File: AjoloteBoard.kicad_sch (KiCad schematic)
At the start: 4 parts, among them SW1 On

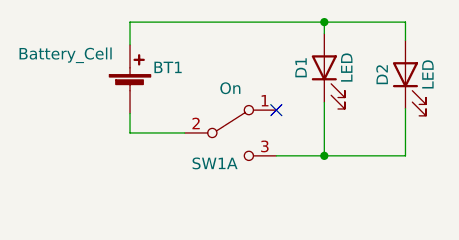
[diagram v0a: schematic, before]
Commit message: Battery holder and switch changed
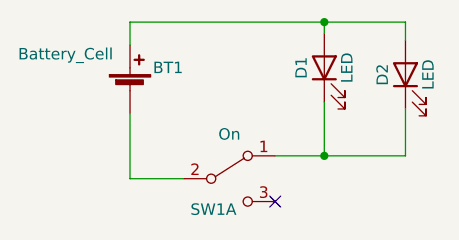
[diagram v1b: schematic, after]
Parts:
- BT1: footprint footprints:79523141 -> Batteries:BAT-HLD-001; manf# (none) -> BAT-HLD-001
- D1, D2: manf# (none) -> Generic LED
- SW1: footprint footprints:Micro_interruptor_SPDT -> footprints:JS102011SAQN; manf# (none) -> JS102011SAQN
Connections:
- net at D1.1 (K), D2.1 (K): now also SW1.1 (A); no longer SW1.3 (C)
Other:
- moved on the sheet: SW1A
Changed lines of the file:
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@@
-(kicad_sch (version 20211123) (generator eeschema)
+(kicad_sch (version 20230121) (generator eeschema)
   (paper "A4")
   (title_block
@@
   (junction (at 120.523 88.265) (diameter 0) (color 0 0 0 0)
   )
-  (no_connect (at 115.189 83.185))
-  (wire (pts (xy 115.189 88.265) (xy 120.523 88.265))
-    (stroke (width 0) (type default) (color 0 0 0 0))
+  (no_connect (at 115.062 93.345))
+  (wire (pts (xy 120.523 88.265) (xy 129.54 88.265))
+    (stroke (width 0) (type default))
   )
-  (wire (pts (xy 120.523 88.265) (xy 129.54 88.265))
-    (stroke (width 0) (type default) (color 0 0 0 0))
+  (wire (pts (xy 115.062 88.265) (xy 120.523 88.265))
+    (stroke (width 0) (type default))
   )
   (wire (pts (xy 129.54 88.265) (xy 129.54 83.058))
-    (stroke (width 0) (type default) (color 0 0 0 0))
+    (stroke (width 0) (type default))
   )
   (wire (pts (xy 120.523 74.676) (xy 120.523 73.406))
-    (stroke (width 0) (type default) (color 0 0 0 0))
+    (stroke (width 0) (type default))
   )
   (wire (pts (xy 120.523 88.265) (xy 120.523 82.296))
-    (stroke (width 0) (type default) (color 0 0 0 0))
+    (stroke (width 0) (type default))
   )
   (wire (pts (xy 129.54 73.406) (xy 129.54 75.438))
-    (stroke (width 0) (type default) (color 0 0 0 0))
+    (stroke (width 0) (type default))
   )
   (wire (pts (xy 98.933 75.946) (xy 98.933 73.406))
-    (stroke (width 0) (type default) (color 0 0 0 0))
+    (stroke (width 0) (type default))
   )
-  (wire (pts (xy 98.933 85.725) (xy 105.029 85.725))
-    (stroke (width 0) (type default) (color 0 0 0 0))
+  (wire (pts (xy 98.933 90.805) (xy 104.902 90.805))
+    (stroke (width 0) (type default))
   )
   (wire (pts (xy 98.933 73.406) (xy 120.523 73.406))
-    (stroke (width 0) (type default) (color 0 0 0 0))
+    (stroke (width 0) (type default))
   )
   (wire (pts (xy 120.523 73.406) (xy 129.54 73.406))
-    (stroke (width 0) (type default) (color 0 0 0 0))
+    (stroke (width 0) (type default))
   )
-  (wire (pts (xy 98.933 83.566) (xy 98.933 85.725))
-    (stroke (width 0) (type default) (color 0 0 0 0))
+  (wire (pts (xy 98.933 83.566) (xy 98.933 90.805))
+    (stroke (width 0) (type default))
   )
   (symbol (lib_id "Device:LED") (at 120.523 78.486 90) (unit 1)
-    (in_bom yes) (on_board yes)
-    (property "Reference" "D1" (id 0) (at 117.983 78.486 0))
-    (property "Value" "LED" (id 1) (at 123.063 78.486 0))
-    (property "Footprint" "LED_THT:LED_D5.0mm_Clear" (id 2) (at 120.523 78.486 0)
+    (in_bom yes) (on_board yes) (dnp no)
+    (property "Reference" "D1" (at 117.983 78.486 0)
+      (effects (font (size 1.27 1.27)))
+    )
+    (property "Value" "LED" (at 123.063 78.486 0)
+      (effects (font (size 1.27 1.27)))
+    )
+    (property "Footprint" "LED_THT:LED_D5.0mm_Clear" (at 120.523 78.486 0)
       (effects (font (size 1.27 1.27)) hide)
     )
-    (property "Datasheet" "" (id 3) (at 120.523 78.486 0))
+    (property "Datasheet" "https://articulo.mercadolibre.com.mx/MLM-849097961-100-led-rgb-camaleon-5mm-parpadeo-rapido-_JM#position=5&search_layout=stack&type=item&tracking_id=6f6aec30-ba55-4563-a3d2-df7b4841300a" (at 120.523 78.486 0)
+      (effects (font (size 1.27 1.27)) hide)
+    )
+    (property "LCSC#" "" (at 120.523 78.486 0)
+      (effects (font (size 1.27 1.27)) hide)
+    )
+    (property "manf#" "Generic LED" (at 120.523 78.486 0)
+      (effects (font (size 1.27 1.27)) hide)
+    )
     (pin "1")
     (pin "2")
+    (instances
+      (project "AjoloteBoard"
+        (path "/7f3eb118-a20c-4239-b800-c9211c66847d"
+          (reference "D1") (unit 1)
+        )
+      )
+    )
   )
   (symbol (lib_id "Device:LED") (at 129.54 79.248 90) (unit 1)
-    (in_bom yes) (on_board yes)
-    (property "Reference" "D2" (id 0) (at 127 79.248 0))
-    (property "Value" "LED" (id 1) (at 132.08 79.248 0))
-    (property "Footprint" "LED_THT:LED_D5.0mm_Clear" (id 2) (at 129.54 79.248 0)
+    (in_bom yes) (on_board yes) (dnp no)
+    (property "Reference" "D2" (at 127 79.248 0)
+      (effects (font (size 1.27 1.27)))
+    )
+    (property "Value" "LED" (at 132.08 79.248 0)
+      (effects (font (size 1.27 1.27)))
+    )
+    (property "Footprint" "LED_THT:LED_D5.0mm_Clear" (at 129.54 79.248 0)
       (effects (font (size 1.27 1.27)) hide)
     )
-    (property "Datasheet" "" (id 3) (at 129.54 79.248 0))
+    (property "Datasheet" "https://articulo.mercadolibre.com.mx/MLM-849097961-100-led-rgb-camaleon-5mm-parpadeo-rapido-_JM#position=5&search_layout=stack&type=item&tracking_id=6f6aec30-ba55-4563-a3d2-df7b4841300a" (at 129.54 79.248 0)
+      (effects (font (size 1.27 1.27)) hide)
+    )
+    (property "LCSC#" "" (at 129.54 79.248 0)
+      (effects (font (size 1.27 1.27)) hide)
+    )
+    (property "manf#" "Generic LED" (at 129.54 79.248 0)
+      (effects (font (size 1.27 1.27)) hide)
+    )
     (pin "1")
     (pin "2")
+    (instances
+      (project "AjoloteBoard"
+        (path "/7f3eb118-a20c-4239-b800-c9211c66847d"
+          (reference "D2") (unit 1)
+        )
+      )
+    )
   )
   (symbol (lib_id "Device:Battery_Cell") (at 98.933 81.026 0) (unit 1)
-    (in_bom yes) (on_board yes)
-    (property "Reference" "BT1" (id 0) (at 101.473 78.486 0)
+    (in_bom yes) (on_board yes) (dnp no)
+    (property "Reference" "BT1" (at 101.473 78.486 0)
       (effects (font (size 1.27 1.27)) (justify left))
     )
-    (property "Value" "Battery_Cell" (id 1) (at 86.487 76.962 0)
+    (property "Value" "Battery_Cell" (at 86.487 76.962 0)
       (effects (font (size 1.27 1.27)) (justify left))
     )
-    (property "Footprint" "footprints:79523141" (id 2) (at 98.933 79.502 90)
+    (property "Footprint" "Batteries:BAT-HLD-001" (at 98.933 79.502 90)
       (effects (font (size 1.27 1.27)) hide)
     )
-    (property "Datasheet" "" (id 3) (at 98.933 79.502 90))
+    (property "Datasheet" "" (at 98.933 79.502 90)
+      (effects (font (size 1.27 1.27)))
+    )
+    (property "LCSC#" "" (at 98.933 81.026 0)
+      (effects (font (size 1.27 1.27)) hide)
+    )
+    (property "manf#" "BAT-HLD-001" (at 98.933 81.026 0)
+      (effects (font (size 1.27 1.27)) hide)
+    )
     (pin "1")
     (pin "2")
+    (instances
+      (project "AjoloteBoard"
+        (path "/7f3eb118-a20c-4239-b800-c9211c66847d"
+          (reference "BT1") (unit 1)
+        )
+      )
+    )
   )
-  (symbol (lib_id "Switch:SW_DPDT_x2") (at 110.109 85.725 0) (unit 1)
-    (in_bom yes) (on_board yes)
-    (property "Reference" "SW1" (id 0) (at 108.331 89.154 0))
-    (property "Value" "On" (id 1) (at 110.109 80.7974 0))
-    (property "Footprint" "footprints:Micro_interruptor_SPDT" (id 2) (at 110.109 85.725 0)
+  (symbol (lib_id "Switch:SW_DPDT_x2") (at 109.982 90.805 0) (unit 1)
+    (in_bom yes) (on_board yes) (dnp no)
+    (property "Reference" "SW1" (at 108.204 94.234 0)
+      (effects (font (size 1.27 1.27)))
+    )
+    (property "Value" "On" (at 109.982 85.8774 0)
+      (effects (font (size 1.27 1.27)))
+    )
+    (property "Footprint" "footprints:JS102011SAQN" (at 109.982 90.805 0)
       (effects (font (size 1.27 1.27)) hide)
     )
-    (property "Datasheet" "~" (id 3) (at 110.109 85.725 0)
+    (property "Datasheet" "~" (at 109.982 90.805 0)
+      (effects (font (size 1.27 1.27)) hide)
+    )
+    (property "LCSC#" "" (at 109.982 90.805 0)
+      (effects (font (size 1.27 1.27)) hide)
+    )
+    (property "manf#" "JS102011SAQN" (at 109.982 90.805 0)
       (effects (font (size 1.27 1.27)) hide)
     )
@@
     (pin "2")
     (pin "3")
+    (pin "4")
+    (pin "5")
+    (pin "6")
+    (instances
+      (project "AjoloteBoard"
+        (path "/7f3eb118-a20c-4239-b800-c9211c66847d"
+          (reference "SW1") (unit 1)
+        )
+      )
+    )
   )
   (sheet_instances
     (path "/" (page "1"))
   )
-  (symbol_instances
-    (path "/00000000-0000-0000-0000-00005af792e6"
-      (reference "BT1") (unit 1) (value "Battery_Cell") (footprint "footprints:79523141")
-    )
-    (path "/00000000-0000-0000-0000-00005af7924c"
-      (reference "D1") (unit 1) (value "LED") (footprint "LED_THT:LED_D5.0mm_Clear")
-    )
-    (path "/00000000-0000-0000-0000-00005af7929c"
-      (reference "D2") (unit 1) (value "LED") (footprint "LED_THT:LED_D5.0mm_Clear")
-    )
-    (path "/00000000-0000-0000-0000-00005da6141c"
-      (reference "SW1") (unit 1) (value "On") (footprint "footprints:Micro_interruptor_SPDT")
-    )
-  )
 )

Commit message: Corrected battery routing
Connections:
- net at D1.2 (A), D2.2 (A): now also BT1.2 (+); no longer BT1.1 (+)
- net at SW1.2 (B): now also BT1.1 (-); no longer BT1.2 (-)
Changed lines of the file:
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@@
       (effects (font (size 1.27 1.27)) hide)
     )
+    (pin "2")
     (pin "1")
-    (pin "2")
     (instances
       (project "AjoloteBoard"
